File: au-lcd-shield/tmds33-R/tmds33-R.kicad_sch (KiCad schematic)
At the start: 15 parts, among them IC1 ME6206A15M3G, IC2 DSLVDS1047PWR, J1 Power, J2 Backlight, J4 Conn_02x09_Odd_Even, U1 UA78M33CDCYR

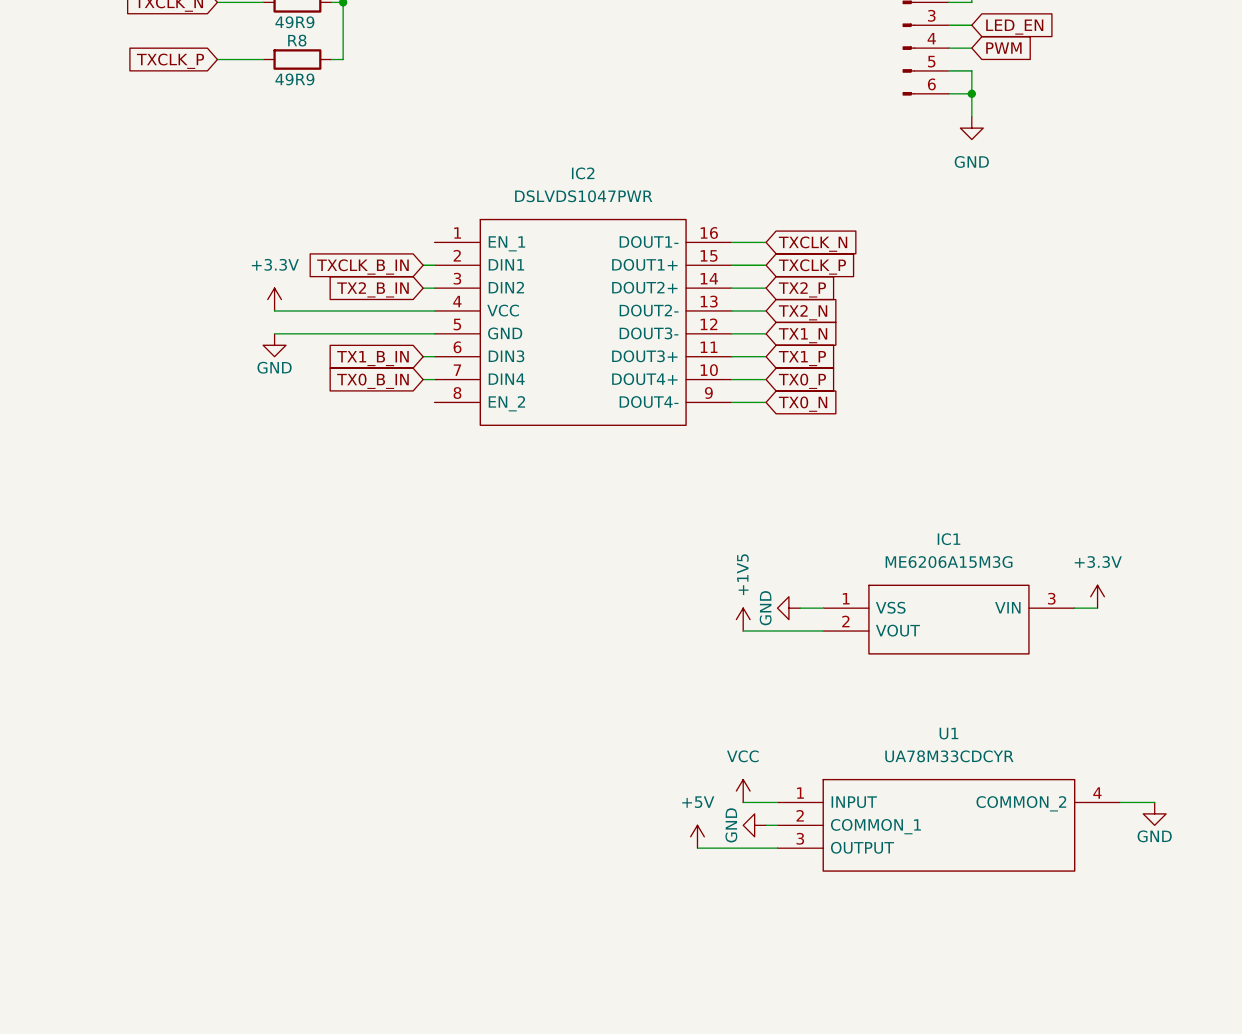
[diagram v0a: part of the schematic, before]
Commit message: add filtering caps for ldo's
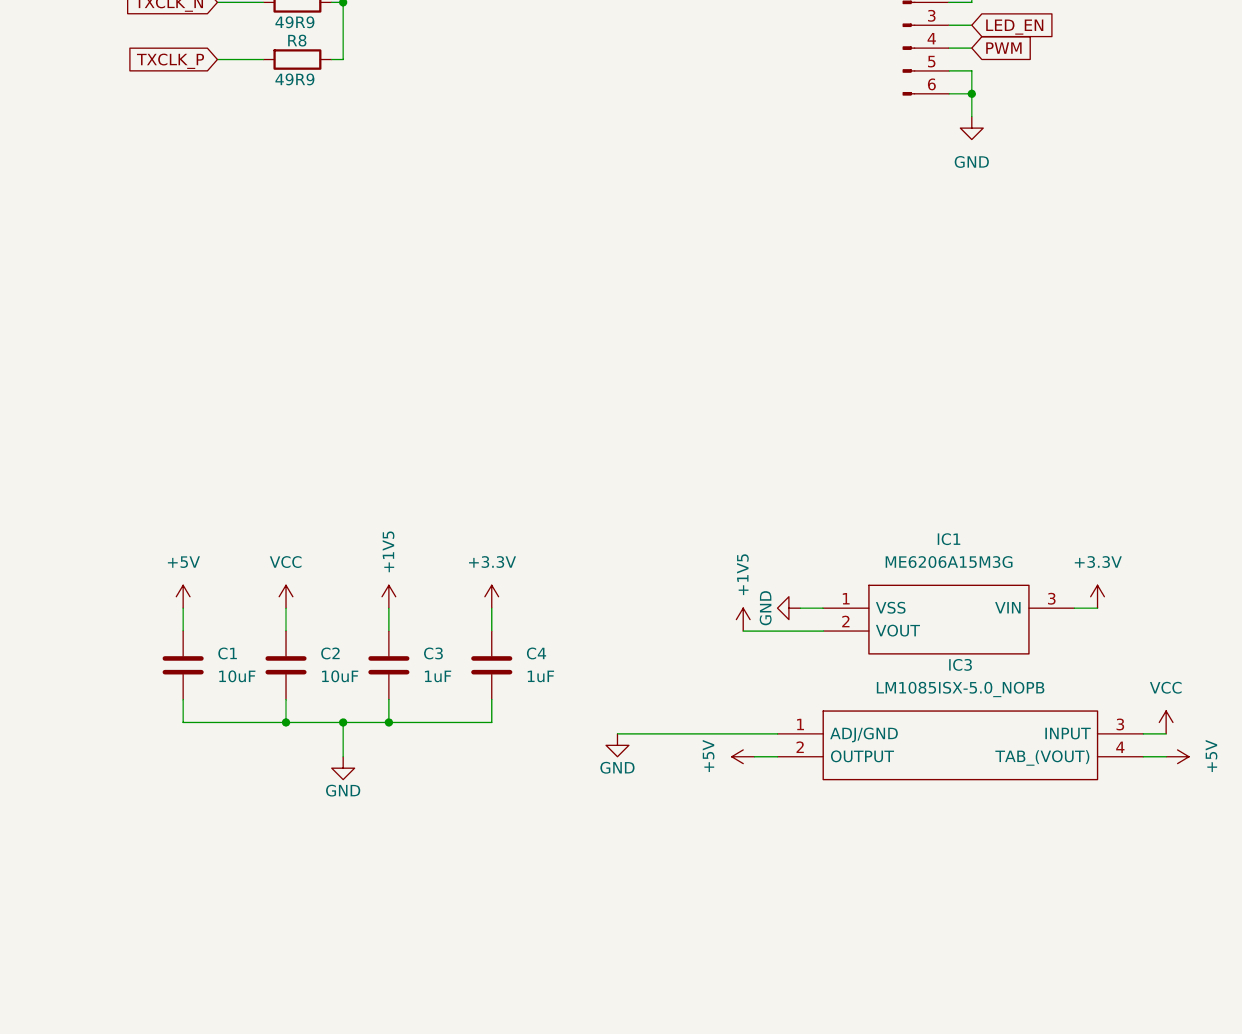
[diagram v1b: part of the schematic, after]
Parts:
- removed IC2: DSLVDS1047PWR, symbol SamacSys_Parts:DSLVDS1047PWR
- removed U1: UA78M33CDCYR, SamacSys_Parts:SOT230P700X180-4N, symbol SamacSys_Parts:UA78M33CDCYR
- added C1, C2: 10uF, Capacitor_SMD:C_0603_1608Metric_Pad1.08x0.95mm_HandSolder, symbol Device:C
- added C3, C4: 1uF, Capacitor_SMD:C_0603_1608Metric_Pad1.08x0.95mm_HandSolder, symbol Device:C
- added IC3: LM1085ISX-5.0_NOPB, SamacSys_Parts:KTT0003B, symbol SamacSys_Parts:LM1085ISX-5.0_NOPB
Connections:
- net +1V5: now also C3.1
- net +3.3V: now also C4.1
- net +5V: now also C1.1, IC3.2 (OUTPUT), IC3.4 (TAB_(VOUT))
- net GND: now also C1.2, C2.2, C3.2, C4.2, IC3.1 (ADJ/GND)
- net VCC: now also C2.1, IC3.3 (INPUT)

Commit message: pcb v1.0
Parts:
- removed IC1: ME6206A15M3G, SamacSys_Parts:SOT95P285X145-3N, symbol SamacSys_Parts:ME6206A30M3G
- removed IC3: LM1085ISX-5.0_NOPB, SamacSys_Parts:KTT0003B, symbol SamacSys_Parts:LM1085ISX-5.0_NOPB
- added U1: ME6206A15M3G, SOT95P285X145-3N, symbol robins-parts:ME6206A15M3G
- added U2: 78M05, Package_TO_SOT_SMD:TO-252-2, symbol Regulator_Linear:IFX27001TFV
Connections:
- net +1V5: now also U1.2 (OUT)
- net +3.3V: now also U1.3 (IN)
- net +5V: now also U2.3 (OUT)
- net GND: now also U1.1 (GND), U2.2 (GND)
- net VCC: now also U2.1 (IN)
